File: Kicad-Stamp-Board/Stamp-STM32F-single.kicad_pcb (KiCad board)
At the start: 2 copper layers, 65 x 42 mm, 35 parts, among them J1 Conn_01x25, J2 Conn_01x25, J3 Conn_01x04, J4 BOOT1, SW1 Reset, SW2 BOOT, U1 STM32F103RET6, U2 ICL3221, Y1 32.768KHz

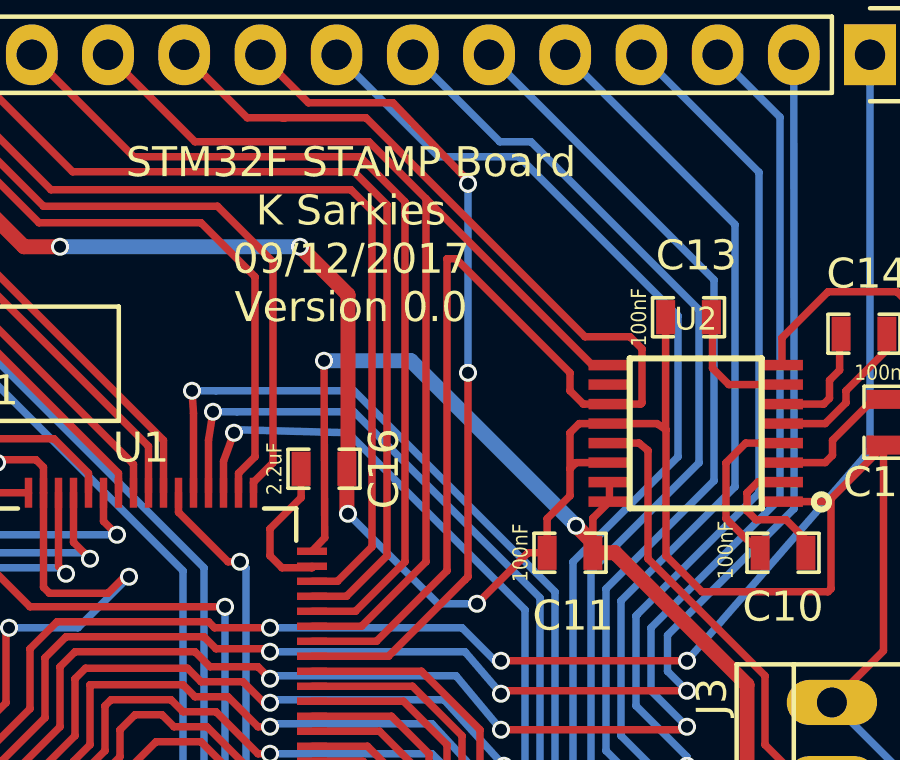
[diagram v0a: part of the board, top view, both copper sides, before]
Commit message: Update PCB to allow more ground fill.
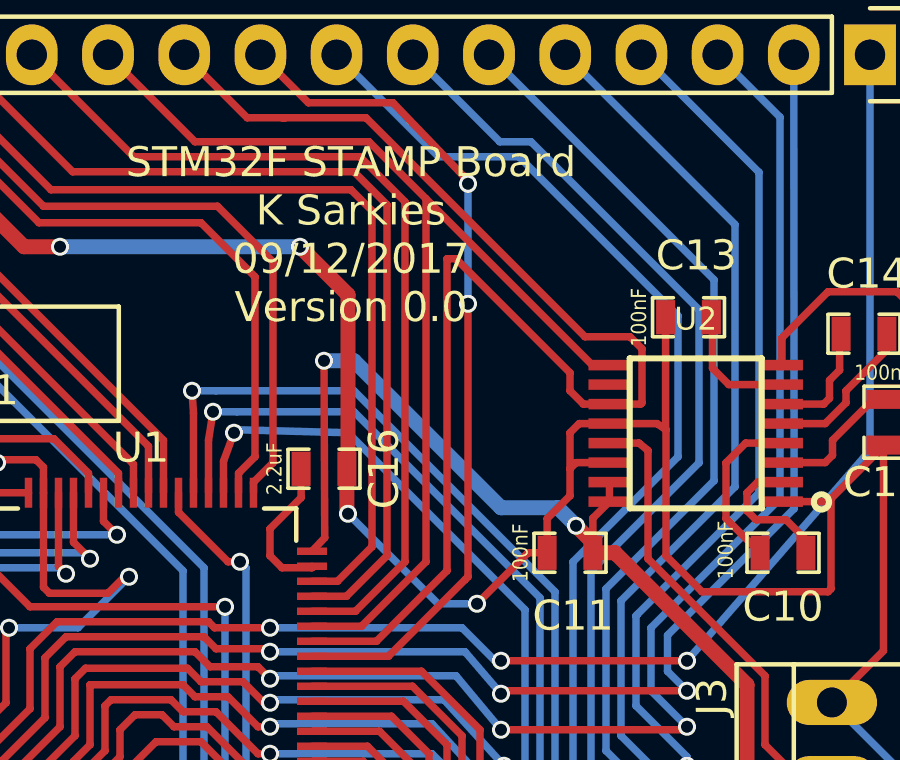
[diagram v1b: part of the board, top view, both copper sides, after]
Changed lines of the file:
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@@
     (thickness 1.6)
     (drawings 5)
-    (tracks 854)
+    (tracks 856)
     (zones 0)
     (modules 35)
@@
   (page A4)
   (layers
-    (0 F.Cu signal)
+    (0 F.Cu signal hide)
     (31 B.Cu signal)
     (32 B.Adhes user hide)
@@
   )
   (setup
-    (last_trace_width 0.5)
+    (last_trace_width 0.25)
     (user_trace_width 0.5)
     (trace_clearance 0.2)
@@
   (segment (start 168.562 92.462) (end 168 91.9) (width 0.5) (layer F.Cu) (net 5))
   (via (at 159.6 86.4) (size 0.6) (drill 0.4) (layers F.Cu B.Cu) (net 5))
-  (segment (start 162.5 86.4) (end 159.6 86.4) (width 0.5) (layer B.Cu) (net 5))
-  (segment (start 168 91.9) (end 162.5 86.4) (width 0.5) (layer B.Cu) (net 5))
+  (segment (start 160.6 86.4) (end 159.6 86.4) (width 0.5) (layer B.Cu) (net 5))
+  (segment (start 168 91.9) (end 167.4 91.3) (width 0.5) (layer B.Cu) (net 5))
+  (segment (start 167.4 91.3) (end 165.5 91.3) (width 0.5) (layer B.Cu) (net 5))
+  (segment (start 165.5 91.3) (end 160.6 86.4) (width 0.5) (layer B.Cu) (net 5))
   (via (at 168 91.9) (size 0.6) (drill 0.4) (layers F.Cu B.Cu) (net 5))
   (segment (start 157.25 102.2) (end 158.4 102.2) (width 0.25) (layer F.Cu) (net 5))
@@
   (segment (start 163.42 79.6) (end 160.02 76.2) (width 0.25) (layer B.Cu) (net 24))
   (segment (start 164.4 80.4) (end 161.9 77.8) (width 0.25) (layer F.Cu) (net 25))
-  (segment (start 164.4 86.8) (end 164.4 93.6) (width 0.25) (layer F.Cu) (net 25))
-  (segment (start 164.4 86.8) (end 164.4 80.5) (width 0.25) (layer B.Cu) (net 25))
+  (segment (start 164.4 84.5) (end 164.4 93.6) (width 0.25) (layer F.Cu) (net 25))
+  (segment (start 164.4 84.5) (end 164.4 80.5) (width 0.25) (layer B.Cu) (net 25))
   (segment (start 161.9 77.8) (end 159.08 77.8) (width 0.25) (layer F.Cu) (net 25))
   (via (at 164.4 80.5) (size 0.6) (drill 0.4) (layers F.Cu B.Cu) (net 25))
-  (via (at 164.4 86.8) (size 0.6) (drill 0.4) (layers F.Cu B.Cu) (net 25))
+  (via (at 164.4 84.5) (size 0.6) (drill 0.4) (layers F.Cu B.Cu) (net 25))
   (segment (start 157.46 76.18) (end 159.08 77.8) (width 0.25) (layer F.Cu) (net 25))
   (segment (start 161.75 96.25) (end 159.2 96.25) (width 0.25) (layer F.Cu) (net 25))

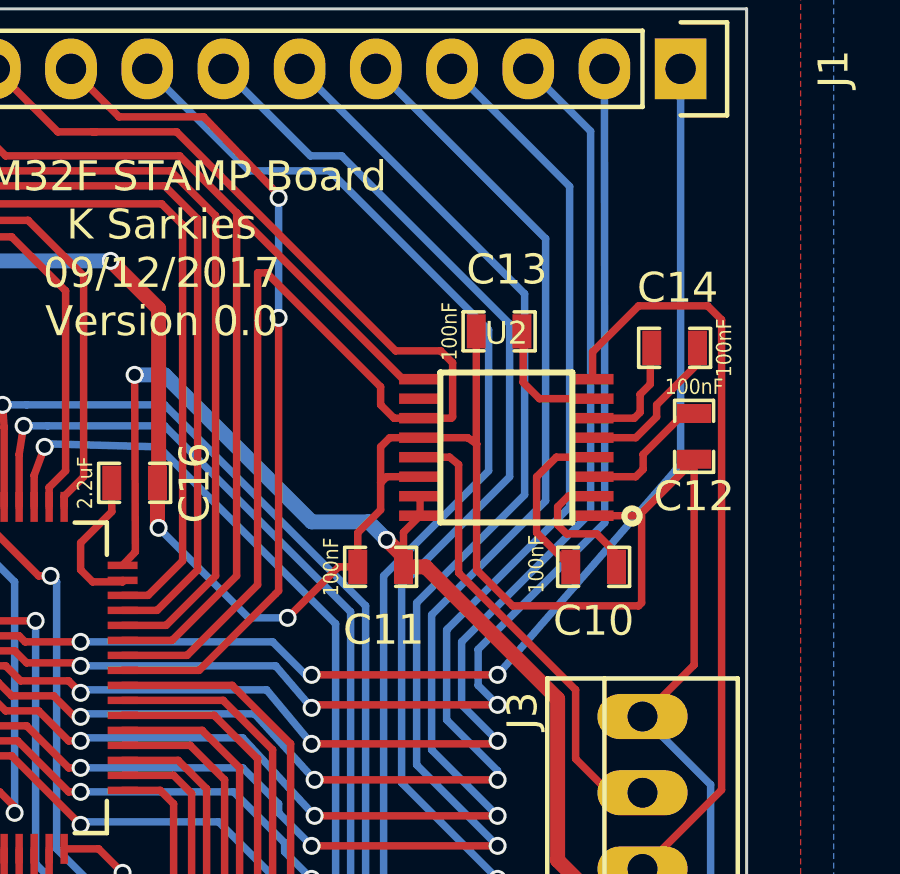
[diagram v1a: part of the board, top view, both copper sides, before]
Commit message: Fix SSOP-16 footprint plus some adjustments to PCB
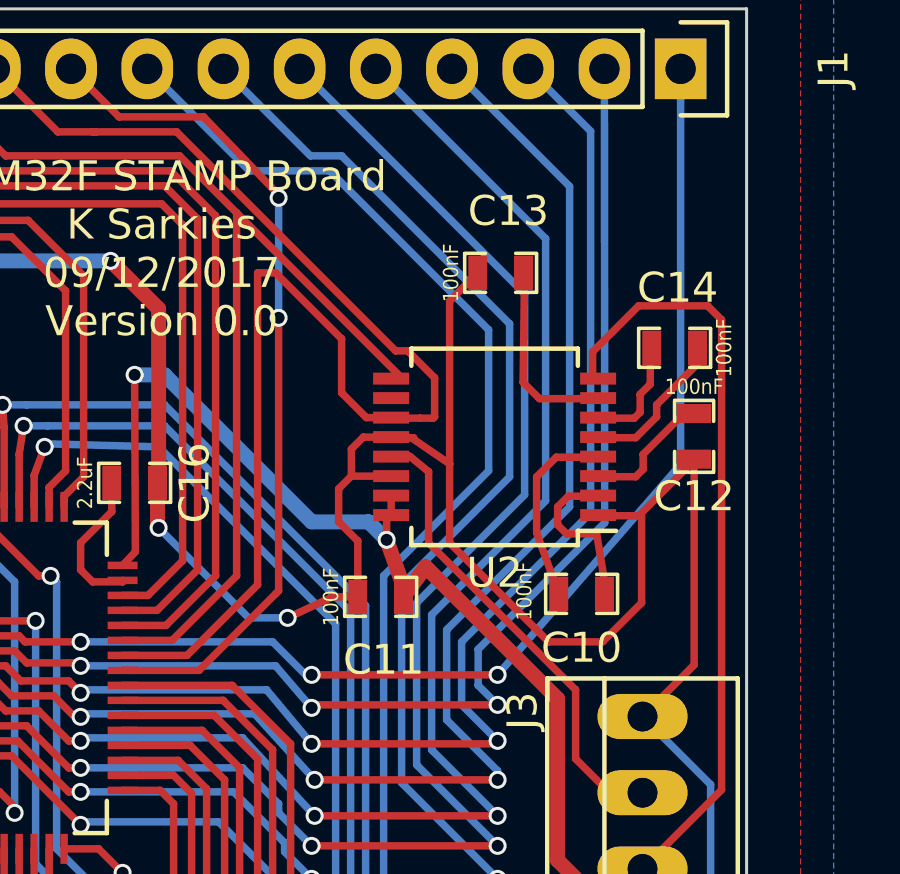
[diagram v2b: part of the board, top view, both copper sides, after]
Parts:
- U2: footprint stamp-stm32f:SSOP16 -> stamp-stm32f:SSOP-16
- moved C13 1.95 mm to (171.8, 83.0)
- moved C11 1.00 mm to (167.8, 93.8)
- moved C10 0.98 mm to (174.5, 93.7)
- moved U2 0.39 mm to (171.6, 88.8)
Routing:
- net Earth: track 267.9 -> 272.5 mm
- net Net-(C13-Pad2): track 4.33 -> 6.28 mm
- net PA9: track 46.0 -> 45.1 mm
- net Net-(C10-Pad1): track 4.71 -> 5.36 mm
- net PA10: track 37.8 -> 37.2 mm
- net Net-(C10-Pad2): track 5.61 -> 6.17 mm

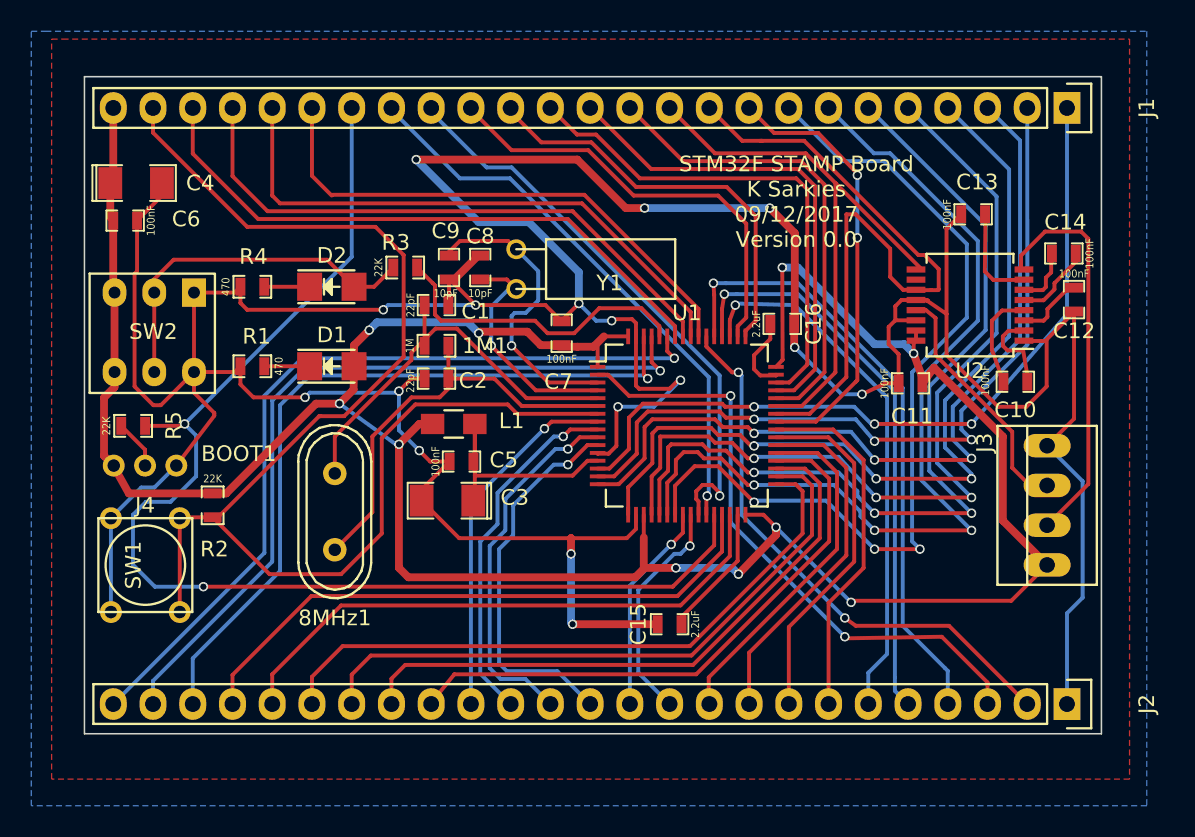
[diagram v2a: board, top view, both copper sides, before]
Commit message: Update PCB to stitch grounds a bit more. Update silk screen. Increase length of PCB to 70mm to satisfy fab house requirements.
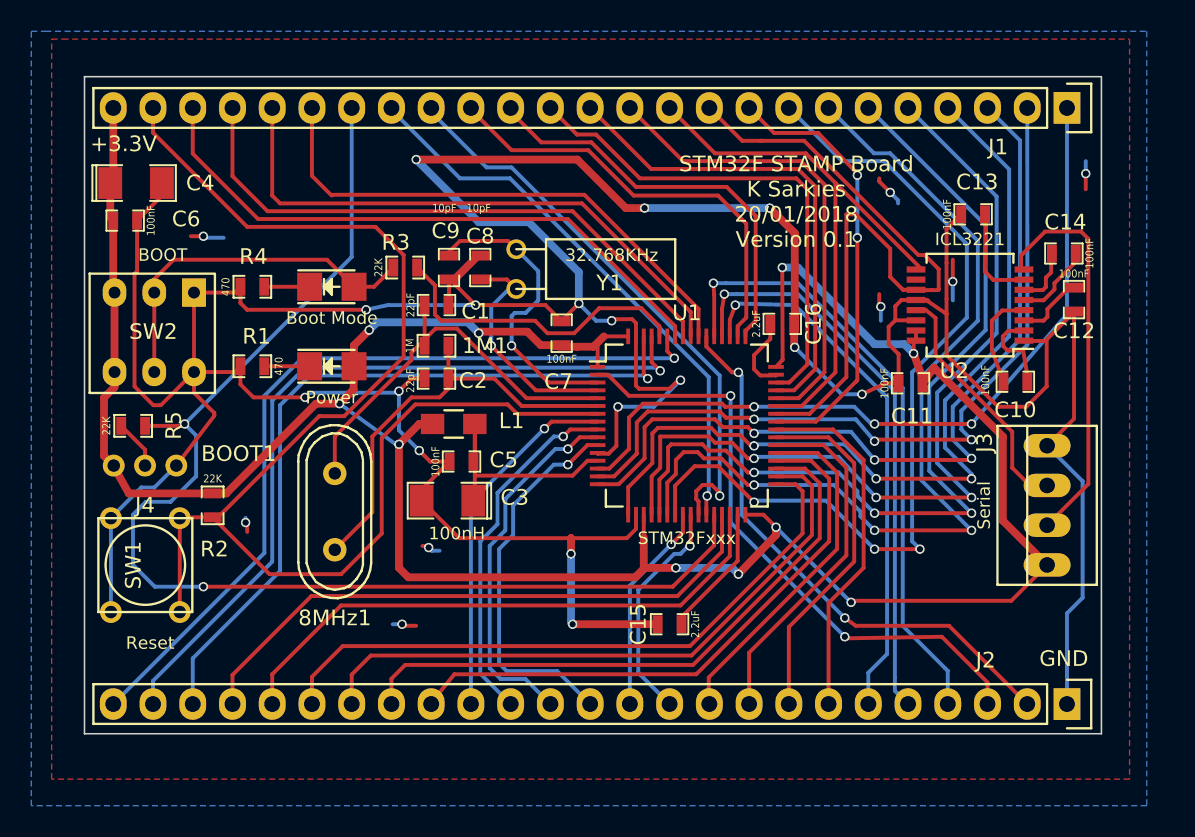
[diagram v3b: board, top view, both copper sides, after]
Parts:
- D1: value LED -> Power
- D2: value LED -> Boot Mode
- J1: value Conn_01x25 -> +3.3V
- J2: value Conn_01x25 -> GND
- J3: value Conn_01x04 -> Serial
- U1: value STM32F103RET6 -> STM32Fxxx
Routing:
- net Earth: track 272.5 -> 286.5 mm, vias 16 -> 24
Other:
- board text added: "STM32F STAMP Board K Sarkies 20/01/2018 Version 0.1"
- board text removed: "STM32F STAMP Board K Sarkies 09/12/2017 Version 0.0"
